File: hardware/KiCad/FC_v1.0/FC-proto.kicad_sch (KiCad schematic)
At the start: 37 parts, among them SW1 SW_SPDT, U1 STM32H743ZIT6, Y2 16MHz

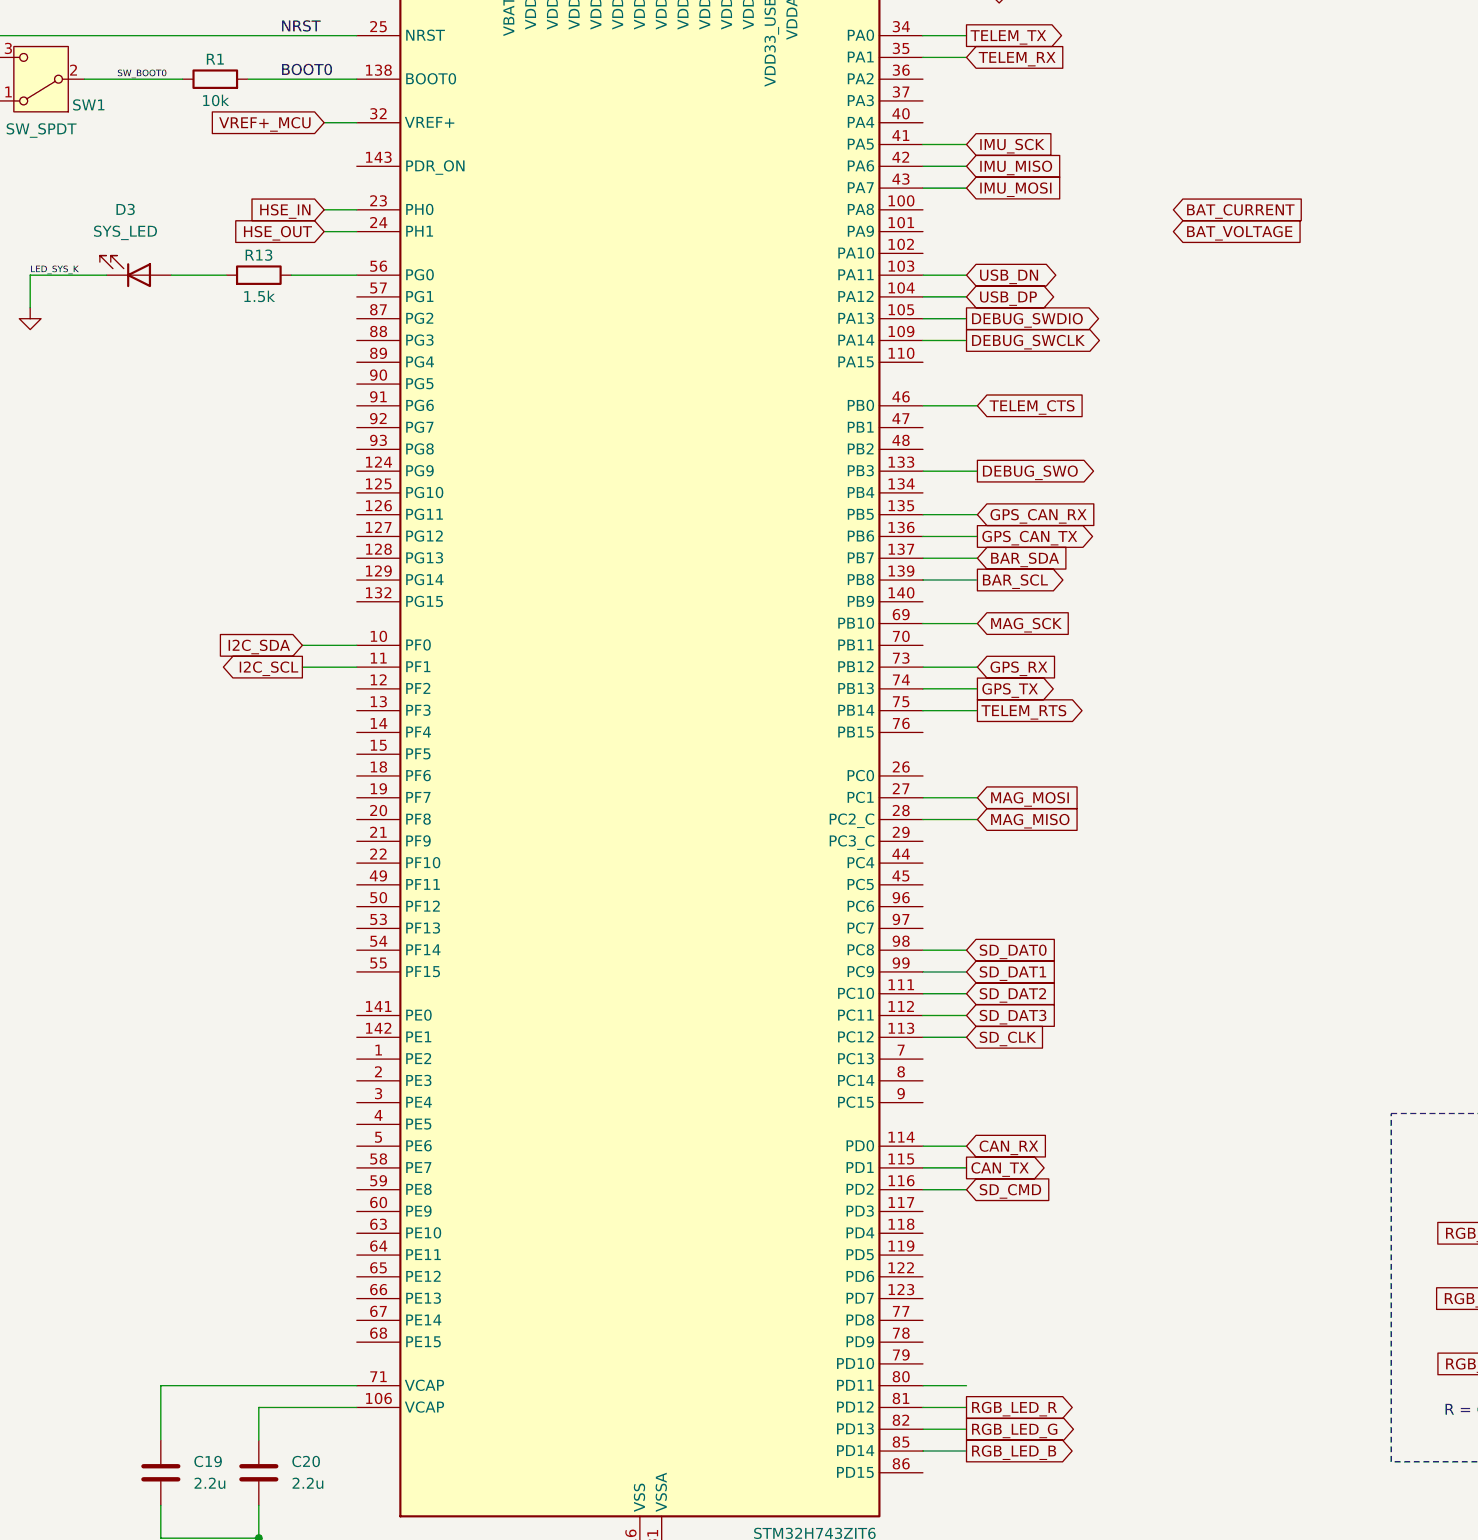
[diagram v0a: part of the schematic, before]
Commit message: Buzzer implementation
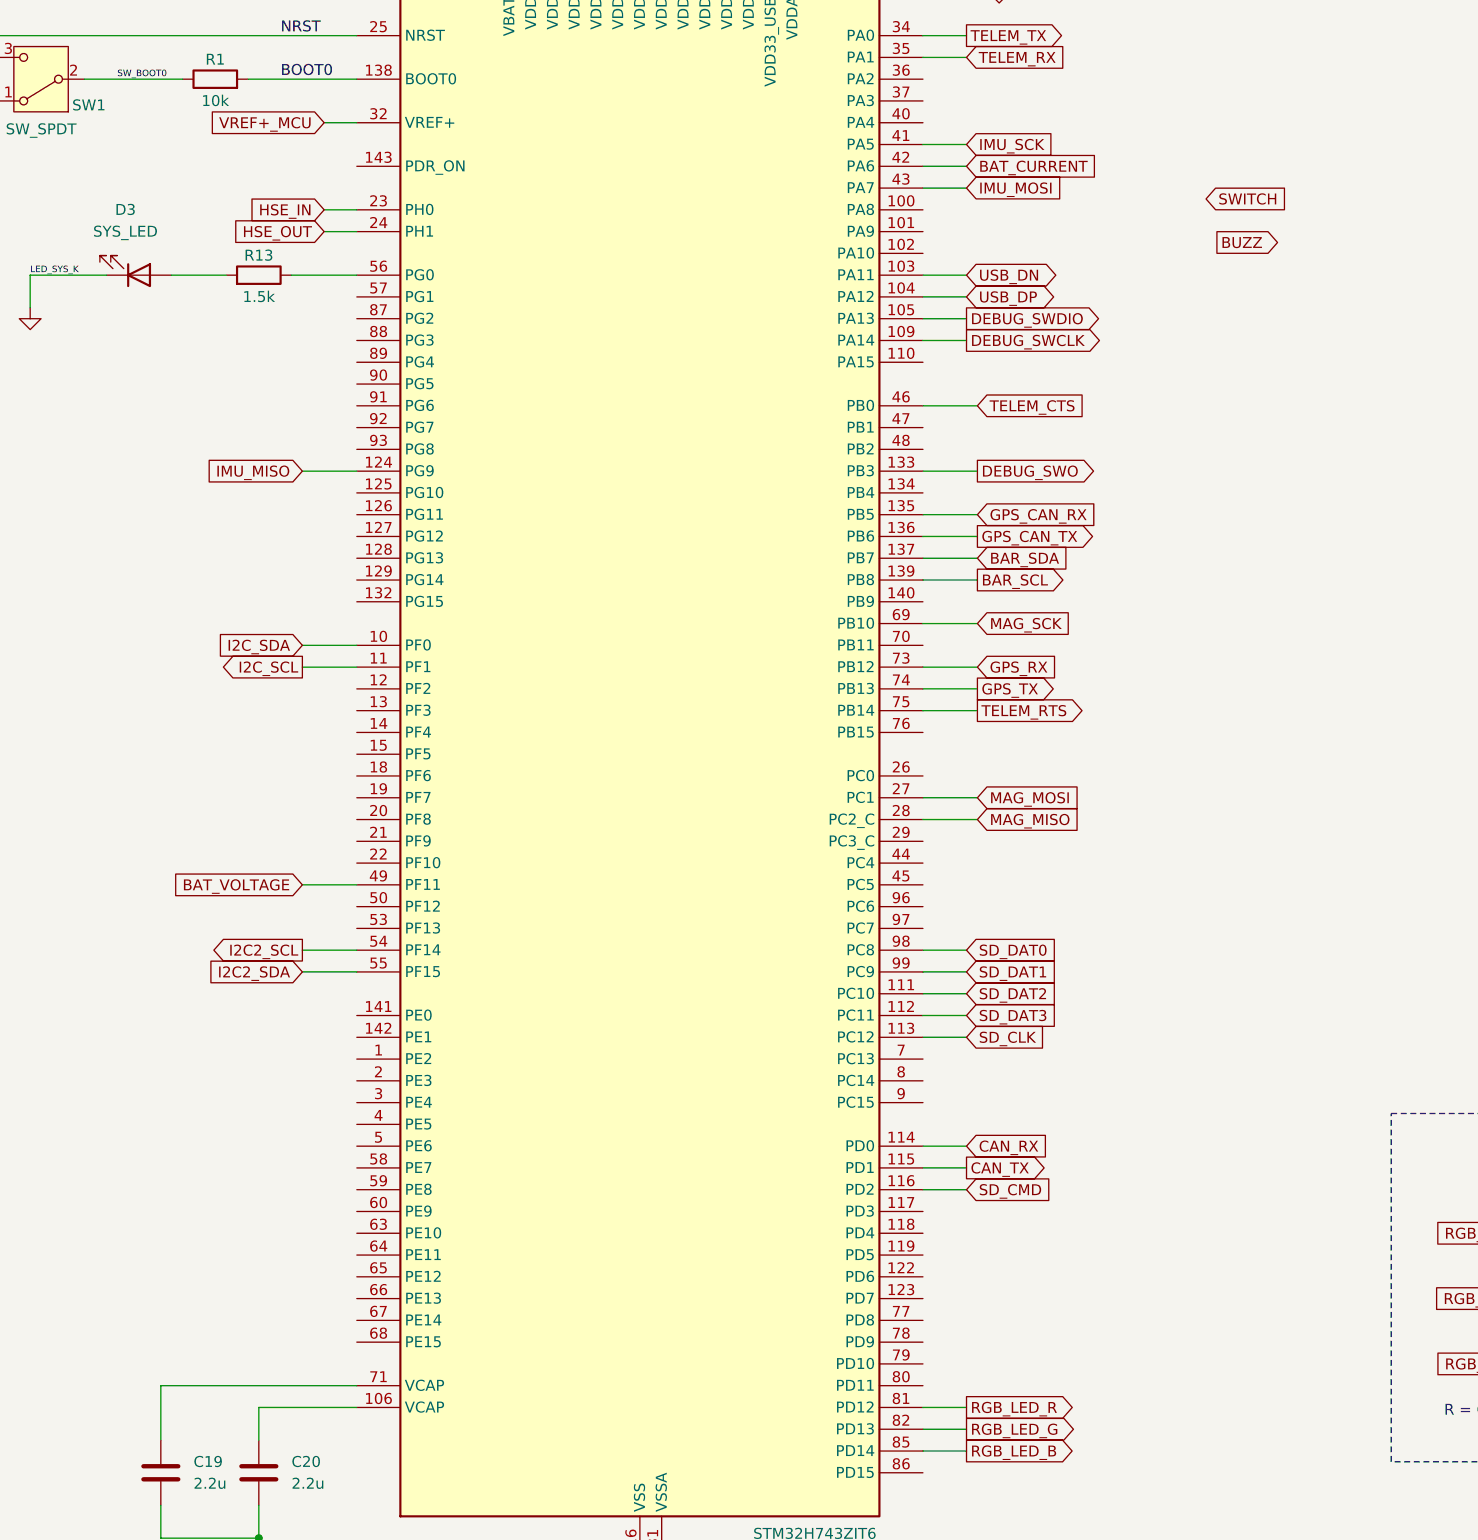
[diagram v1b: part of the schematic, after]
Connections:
- net BAT_CURRENT: now also U1.42 (PA6)
- net BAT_VOLTAGE: now also U1.49 (PF11)
- net IMU_MISO: now also U1.124 (PG9); no longer U1.42 (PA6)
- net I2C2_SCL: now reaches U1.54 (PF14)
- net I2C2_SDA: now reaches U1.55 (PF15)
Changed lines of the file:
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@@
+	(wire
+		(pts
+			(xy 166.37 105.41) (xy 172.72 105.41)
+		)
+		(stroke
+			(width 0)
+			(type default)
+		)
+	)
 	(wire
 		(pts
@@
 	(wire
 		(pts
-			(xy 238.76 212.09) (xy 243.84 212.09)
-		)
-		(stroke
-			(width 0)
-			(type default)
-		)
-	)
-	(wire
-		(pts
 			(xy 69.85 146.05) (xy 69.85 147.32)
 		)
@@
 	(wire
 		(pts
+			(xy 238.76 69.85) (xy 243.84 69.85)
+		)
+		(stroke
+			(width 0)
+			(type default)
+		)
+	)
+	(wire
+		(pts
 			(xy 198.12 41.91) (xy 198.12 44.45)
 		)
@@
 	(wire
 		(pts
+			(xy 166.37 163.83) (xy 172.72 163.83)
+		)
+		(stroke
+			(width 0)
+			(type default)
+		)
+	)
+	(wire
+		(pts
 			(xy 166.37 125.73) (xy 172.72 125.73)
 		)
@@
 	(wire
 		(pts
+			(xy 166.37 161.29) (xy 172.72 161.29)
+		)
+		(stroke
+			(width 0)
+			(type default)
+		)
+	)
+	(wire
+		(pts
 			(xy 69.85 156.21) (xy 80.01 156.21)
 		)
@@
 	(wire
 		(pts
-			(xy 238.76 69.85) (xy 243.84 69.85)
-		)
-		(stroke
-			(width 0)
-			(type default)
-		)
-	)
-	(wire
-		(pts
 			(xy 238.76 105.41) (xy 245.11 105.41)
 		)
@@
 		(pts
 			(xy 73.66 140.97) (xy 80.01 140.97)
+		)
+		(stroke
+			(width 0)
+			(type default)
+		)
+	)
+	(wire
+		(pts
+			(xy 166.37 153.67) (xy 172.72 153.67)
 		)
 		(stroke
@@
 		)
 	)
+	(global_label "I2C2_SCL"
+		(shape output)
+		(at 166.37 161.29 180)
+		(fields_autoplaced yes)
+		(effects
+			(font
+				(size 1.27 1.27)
+			)
+			(justify right)
+		)
+		(property "Intersheetrefs" "${INTERSHEET_REFS}"
+			(at 154.6158 161.29 0)
+			(effects
+				(font
+					(size 1.27 1.27)
+				)
+				(justify right)
+				(hide yes)
+			)
+		)
+	)
 	(global_label "VREF+_MCU"
 		(shape input)
@@
 	(global_label "BAT_CURRENT"
 		(shape input)
-		(at 267.97 74.93 0)
-		(fields_autoplaced yes)
-		(effects
-			(font
-				(size 1.27 1.27)
-			)
-			(justify left)
-		)
-		(property "Intersheetrefs" "${INTERSHEET_REFS}"
-			(at 283.8366 74.93 0)
+		(at 243.84 69.85 0)
+		(fields_autoplaced yes)
+		(effects
+			(font
+				(size 1.27 1.27)
+			)
+			(justify left)
+		)
+		(property "Intersheetrefs" "${INTERSHEET_REFS}"
+			(at 259.7066 69.85 0)
 			(effects
 				(font
@@
 				)
 				(justify left)
+				(hide yes)
+			)
+		)
+	)
+	(global_label "I2C2_SDA"
+		(shape input)
+		(at 166.37 163.83 180)
+		(fields_autoplaced yes)
+		(effects
+			(font
+				(size 1.27 1.27)
+			)
+			(justify right)
+		)
+		(property "Intersheetrefs" "${INTERSHEET_REFS}"
+			(at 154.5553 163.83 0)
+			(effects
+				(font
+					(size 1.27 1.27)
+				)
+				(justify right)
 				(hide yes)
 			)
@@
 		)
 	)
+	(global_label "SWITCH"
+		(shape input)
+		(at 271.78 73.66 0)
+		(fields_autoplaced yes)
+		(effects
+			(font
+				(size 1.27 1.27)
+			)
+			(justify left)
+		)
+		(property "Intersheetrefs" "${INTERSHEET_REFS}"
+			(at 281.599 73.66 0)
+			(effects
+				(font
+					(size 1.27 1.27)
+				)
+				(justify left)
+				(hide yes)
+			)
+		)
+	)
 	(global_label "RGB_LED_B"
 		(shape output)
@@
 		)
 	)
+	(global_label "BUZZ"
+		(shape output)
+		(at 273.05 78.74 0)
+		(fields_autoplaced yes)
+		(effects
+			(font
+				(size 1.27 1.27)
+			)
+			(justify left)
+		)
+		(property "Intersheetrefs" "${INTERSHEET_REFS}"
+			(at 281.0547 78.74 0)
+			(effects
+				(font
+					(size 1.27 1.27)
+				)
+				(justify left)
+				(hide yes)
+			)
+		)
+	)
 	(global_label "RGB_LED_B"
 		(shape input)
@@
 	(global_label "IMU_MISO"
 		(shape input)
-		(at 243.84 69.85 0)
-		(fields_autoplaced yes)
-		(effects
-			(font
-				(size 1.27 1.27)
-			)
-			(justify left)
-		)
-		(property "Intersheetrefs" "${INTERSHEET_REFS}"
-			(at 255.7757 69.85 0)
-			(effects
-				(font
-					(size 1.27 1.27)
-				)
-				(justify left)
+		(at 166.37 105.41 180)
+		(fields_autoplaced yes)
+		(effects
+			(font
+				(size 1.27 1.27)
+			)
+			(justify right)
+		)
+		(property "Intersheetrefs" "${INTERSHEET_REFS}"
+			(at 154.4343 105.41 0)
+			(effects
+				(font
+					(size 1.27 1.27)
+				)
+				(justify right)
 				(hide yes)
 			)
@@
 	(global_label "BAT_VOLTAGE"
 		(shape input)
-		(at 267.97 77.47 0)
-		(fields_autoplaced yes)
-		(effects
-			(font
-				(size 1.27 1.27)
-			)
-			(justify left)
-		)
-		(property "Intersheetrefs" "${INTERSHEET_REFS}"
-			(at 283.1714 77.47 0)
-			(effects
-				(font
-					(size 1.27 1.27)
-				)
-				(justify left)
-				(hide yes)
-			)
+		(at 166.37 153.67 180)
+		(fields_autoplaced yes)
+		(effects
+			(font
+				(size 1.27 1.27)
+			)
+			(justify right)
+		)
+		(property "Intersheetrefs" "${INTERSHEET_REFS}"
+			(at 151.1686 153.67 0)
+			(effects
+				(font
+					(size 1.27 1.27)
+				)
+				(justify right)
+				(hide yes)
+			)

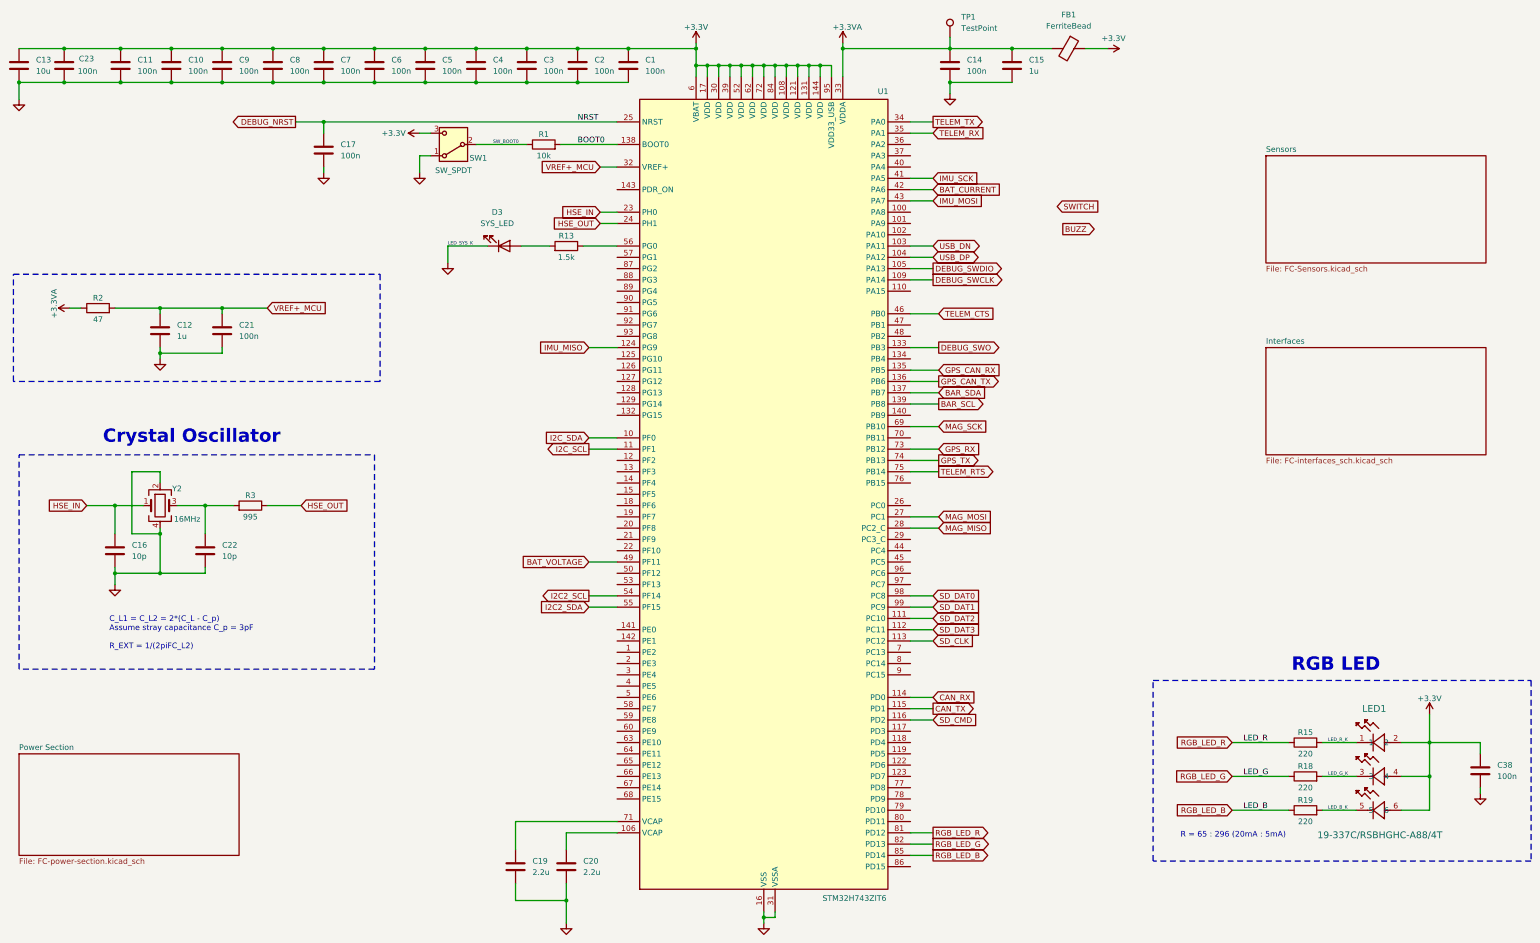
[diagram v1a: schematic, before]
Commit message: ESC PWM Generation
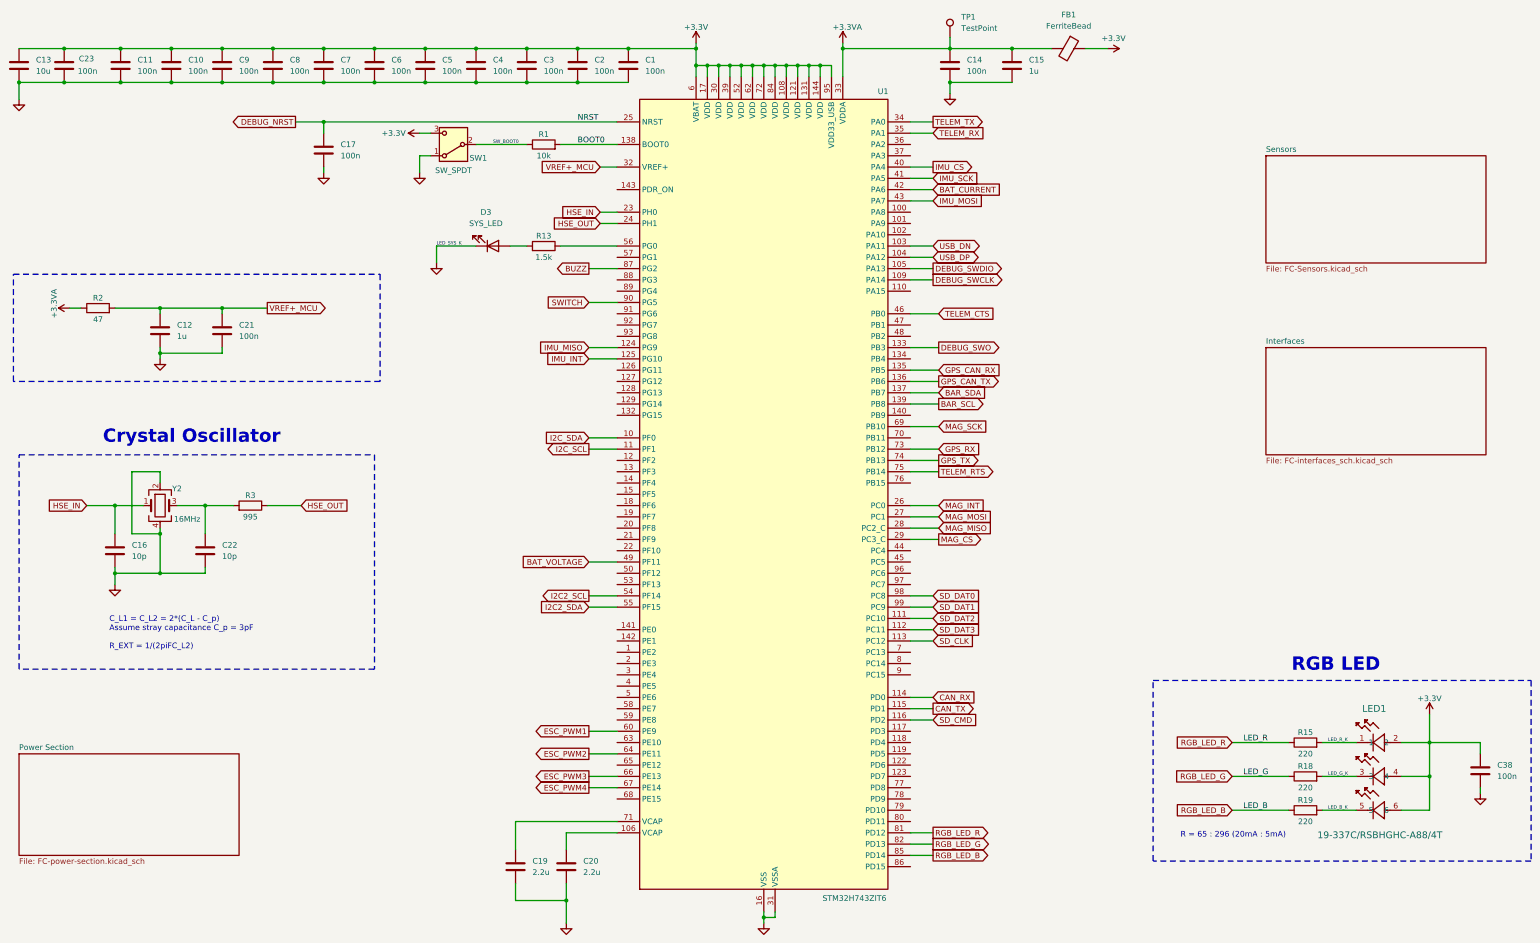
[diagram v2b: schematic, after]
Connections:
- net BUZZ: now also U1.87 (PG2)
- net SWITCH: now also U1.90 (PG5)
- net IMU_INT: now reaches U1.125 (PG10)
- net MAG_INT: now reaches U1.26 (PC0)
- net MAG_CS: now reaches U1.29 (PC3_C)
- net IMU_CS: now reaches U1.40 (PA4)
- net ESC_PWM1: now reaches U1.60 (PE9)
- net ESC_PWM2: now reaches U1.64 (PE11)
- net ESC_PWM3: now reaches U1.66 (PE13)
- net ESC_PWM4: now reaches U1.67 (PE14)
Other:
- moved on the sheet: D3, R13
